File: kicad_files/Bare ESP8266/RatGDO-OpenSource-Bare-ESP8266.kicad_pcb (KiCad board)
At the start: 2 copper layers, 55 x 82.7 mm, 24 parts, among them J1 Screw_Terminal_01x03, J2 Screw_Terminal_01x03, J3 Screw_Terminal_01x03, J4 Conn_01x04, J5 Screw_Terminal_01x02, J6 Conn_01x02, Q1 2N7002, Q2 AO3400A, SW1 SW_Push, U1 ESP-12F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

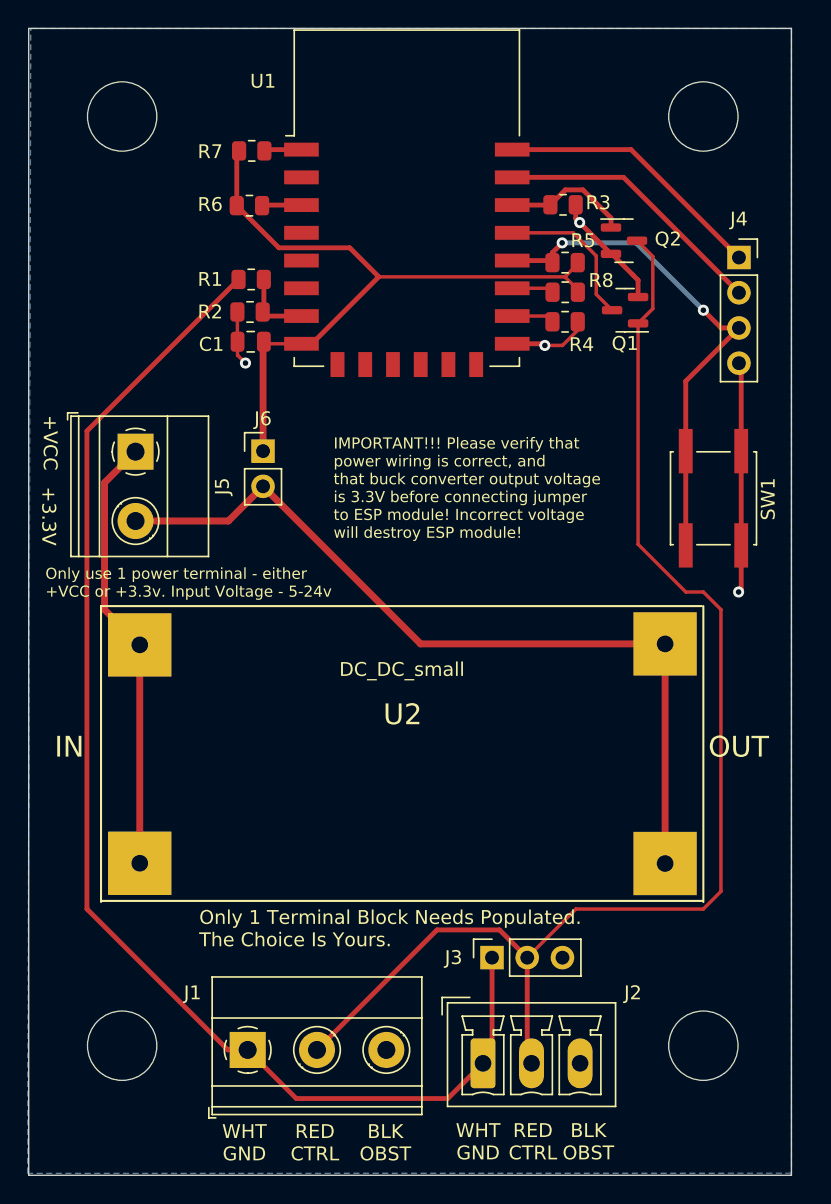
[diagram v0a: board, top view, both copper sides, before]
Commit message: Missed Silkscreening for programming header
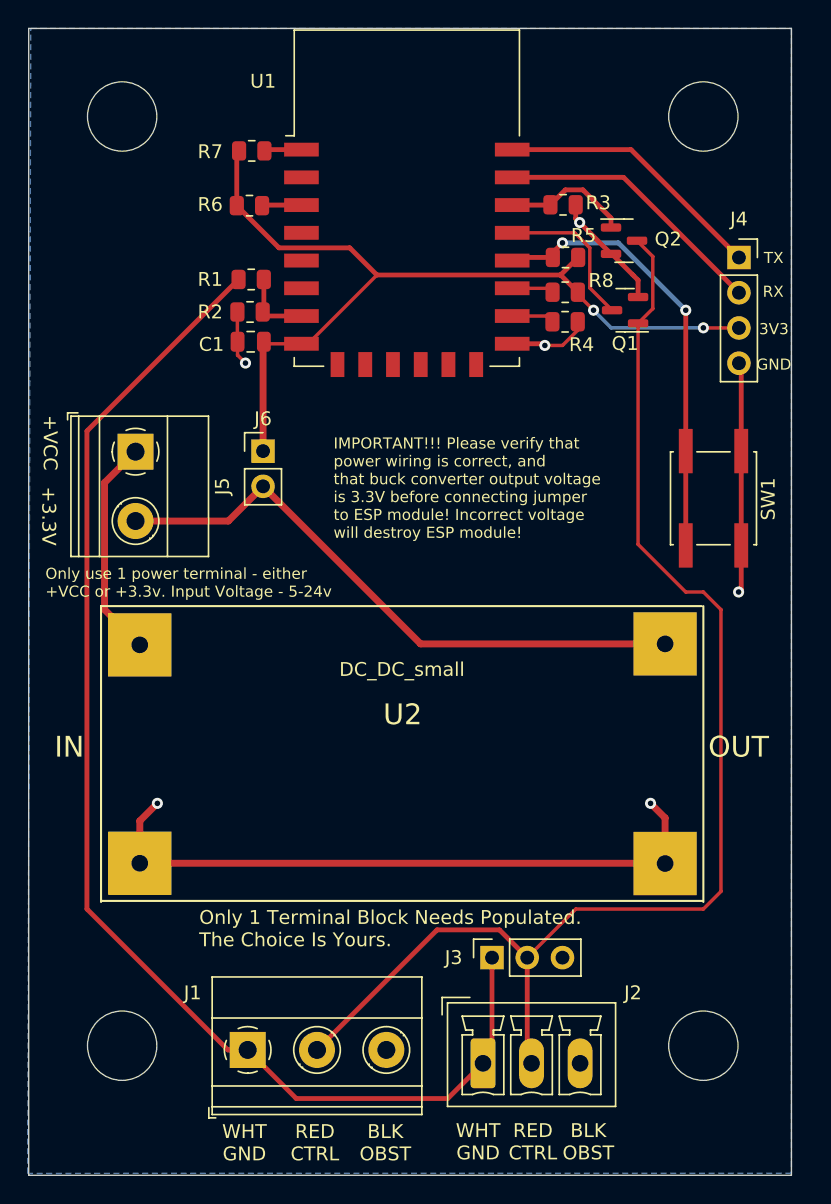
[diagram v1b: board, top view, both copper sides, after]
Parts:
- moved R5 0.38 mm to (152.6, 73.7)
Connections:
- J4 pad 3: Net-(J4-Pin_3) -> +3.3V
- R5 pad 1: Net-(J4-Pin_3) -> Net-(U1-GPIO0)
- SW1 pad 2: Net-(J4-Pin_3) -> Net-(U1-GPIO0)
- U1 pad 18: Net-(J4-Pin_3) -> Net-(U1-GPIO0)
- U2 pad 2: +12V -> GND
- U2 pad 4: Net-(J5-+3.3V) -> GND
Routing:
- net GND: track 35.2 -> 82.8 mm, vias 4 -> 6
- net Net-(J4-Pin_3): track 37.2 -> 0.00 mm, vias 2 -> 0
- net Net-(U1-GPIO0): track 0.00 -> 32.4 mm, vias 0 -> 2
- net Net-(J5-+3.3V): track 59.8 -> 43.9 mm
- net +12V: track 31.7 -> 15.9 mm
- net +3.3V: track 51.1 -> 65.1 mm, vias 0 -> 2
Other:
- board text added: "3V3"
- board text added: "GND"
- board text added: "RX"
- board text added: "TX"

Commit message: Updated Trace widths
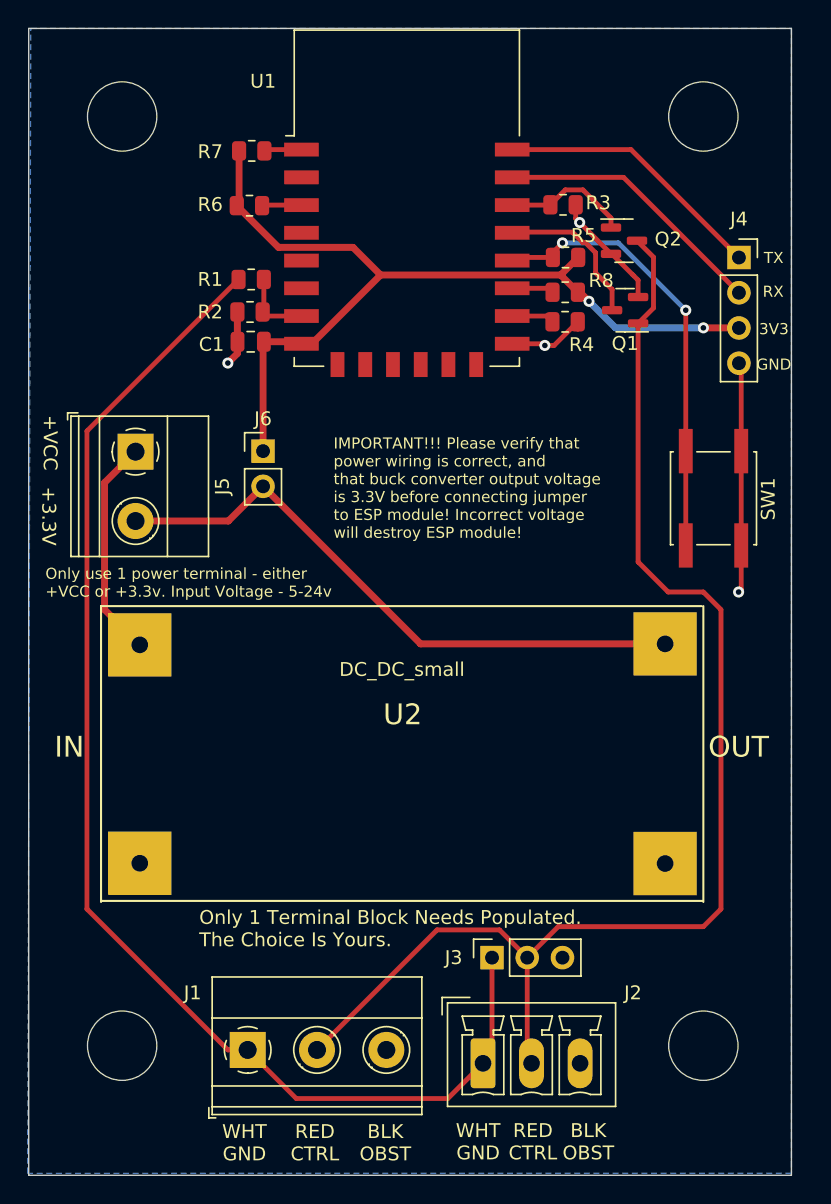
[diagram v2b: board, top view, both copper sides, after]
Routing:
- net GND: track 82.8 -> 35.6 mm, vias 6 -> 4
- net Net-(J1-RED/CTRL): track 94.3 -> 95.9 mm
- net +3.3V: track 65.1 -> 65.6 mm

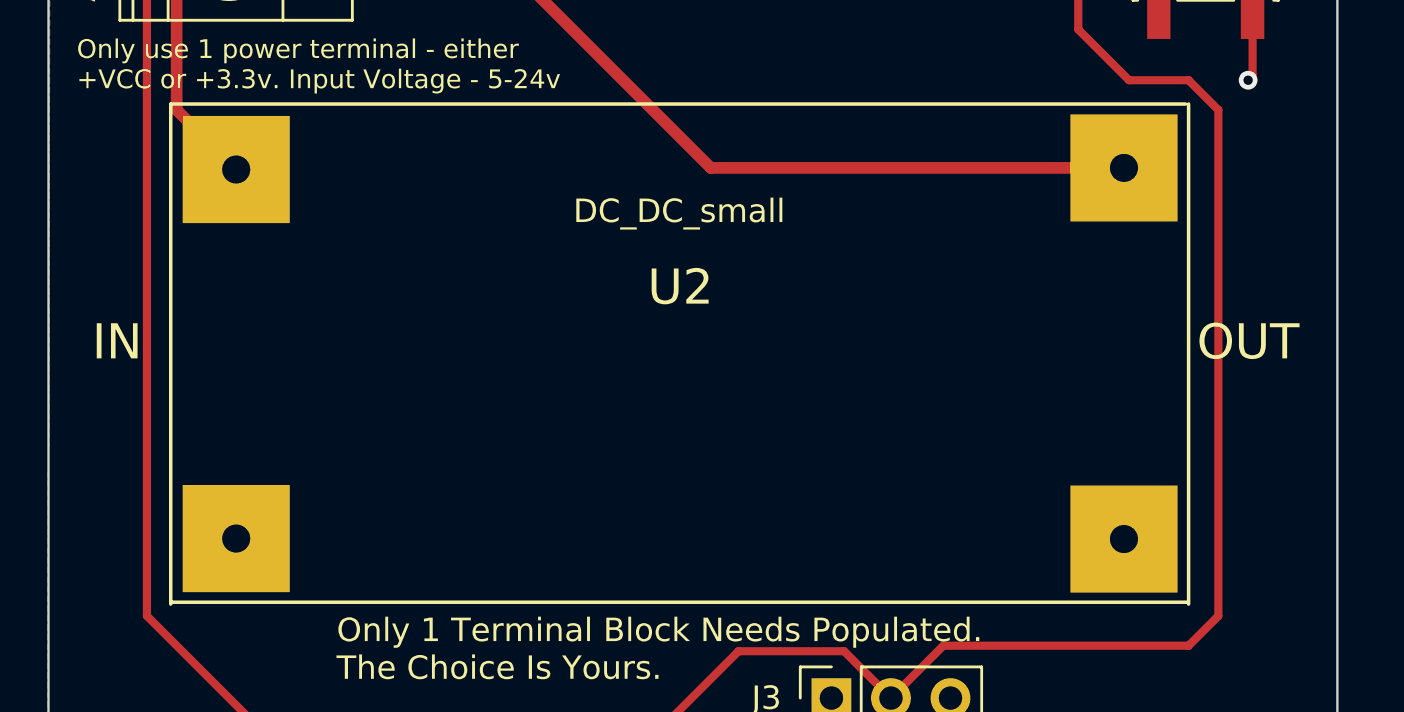
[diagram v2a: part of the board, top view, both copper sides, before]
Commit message: Added silkscreen to LM2596 area to aid in placement.
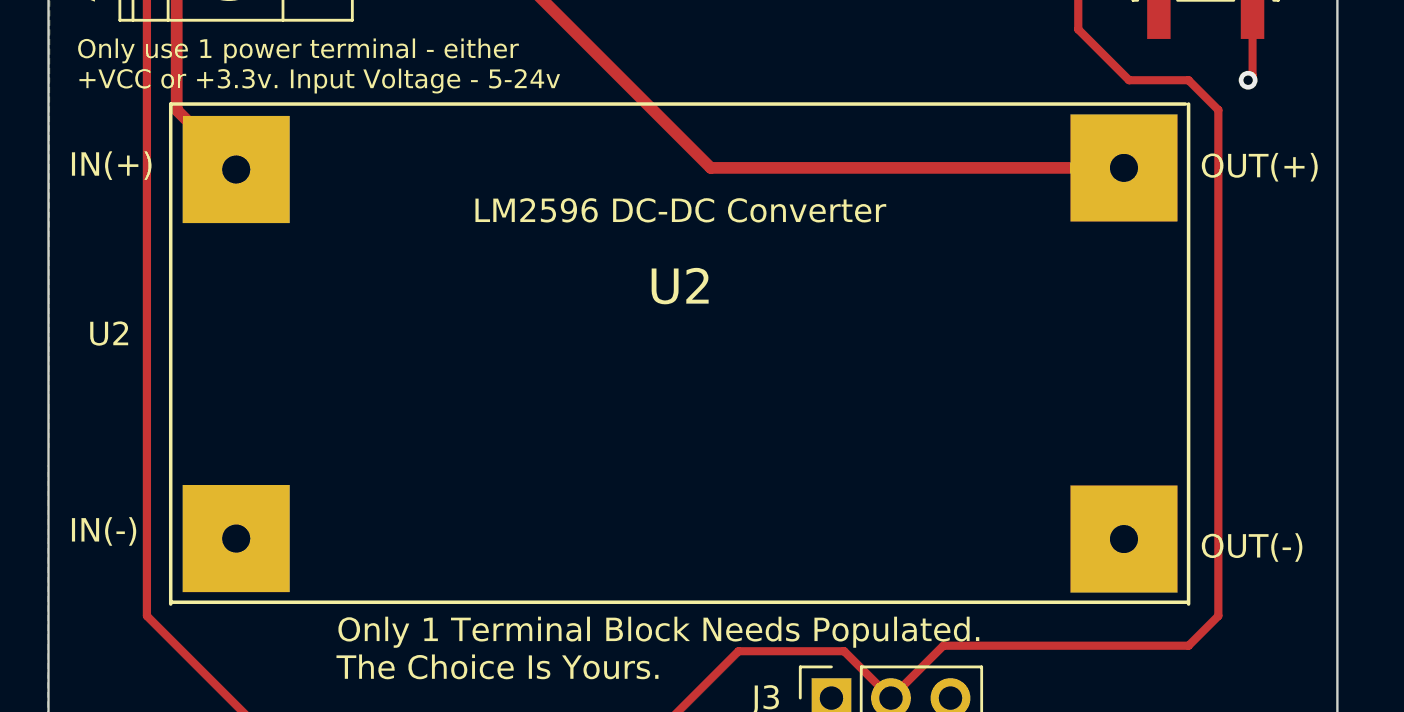
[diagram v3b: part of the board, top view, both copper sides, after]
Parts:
- U2: value DC_DC_small -> LM2596 DC-DC Converter
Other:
- board text added: "IN(+)"
- board text added: "IN(-)"
- board text added: "OUT(+)"
- board text added: "OUT(-)"
- board text added: "U2"
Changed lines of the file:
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@@
         (effects (font (size 1.5 1.5) (thickness 0.15)))
     )
-    (fp_text value "DC_DC_small" (at 0.0508 -5.588) (layer "F.SilkS")
-        (effects (font (size 1 1) (thickness 0.15)))
-    )
-    (fp_text user "IN" (at -23.9355 0) (layer "F.SilkS")
-        (effects (font (size 1.5 1.5) (thickness 0.15)))
-    )
-    (fp_text user "OUT" (at 24.3245 0) (layer "F.SilkS")
-        (effects (font (size 1.5 1.5) (thickness 0.15)))
+    (fp_text value "LM2596 DC-DC Converter" (at 0.0508 -5.588) (layer "F.SilkS")
+        (effects (font (size 1 1) (thickness 0.15)))
     )
     (fp_line (start -21.6495 -10.16) (end 21.6495 -10.16)
@@
     (effects (font (size 1 1) (thickness 0.15)) (justify bottom))
   )
+  (gr_text "IN(+)" (at 114.774765 101.986489) (layer "F.SilkS")
+    (effects (font (size 1 1) (thickness 0.15)) (justify left bottom))
+  )
   (gr_text "GND" (at 166.390265 81.852093) (layer "F.SilkS")
     (effects (font (size 0.8 0.8) (thickness 0.15)) (justify left bottom))
@@
     (effects (font (size 1 1) (thickness 0.15)) (justify left bottom))
   )
+  (gr_text "IN(-)" (at 114.774765 117.597697) (layer "F.SilkS")
+    (effects (font (size 1 1) (thickness 0.15)) (justify left bottom))
+  )
   (gr_text "BLK\nOBST" (at 139.626103 138.894836) (layer "F.SilkS")
     (effects (font (size 1 1) (thickness 0.15)) (justify bottom))
   )
+  (gr_text "U2" (at 115.57 109.22) (layer "F.SilkS")
+    (effects (font (size 1 1) (thickness 0.15)) (justify left bottom))
+  )
+  (gr_text "OUT(-)" (at 163.046266 118.2824) (layer "F.SilkS")
+    (effects (font (size 1 1) (thickness 0.15)) (justify left bottom))
+  )
   (gr_text "+VCC" (at 114.874616 85.028219 270) (layer "F.SilkS")
     (effects (font (size 1 1) (thickness 0.15)) (justify left bottom))
@@
     (effects (font (size 0.8 0.8) (thickness 0.15)) (justify left bottom))
   )
+  (gr_text "OUT(+)" (at 163.046266 102.054959) (layer "F.SilkS")
+    (effects (font (size 1 1) (thickness 0.15)) (justify left bottom))
+  )
   (gr_text "RX" (at 166.83659 76.597638) (layer "F.SilkS")

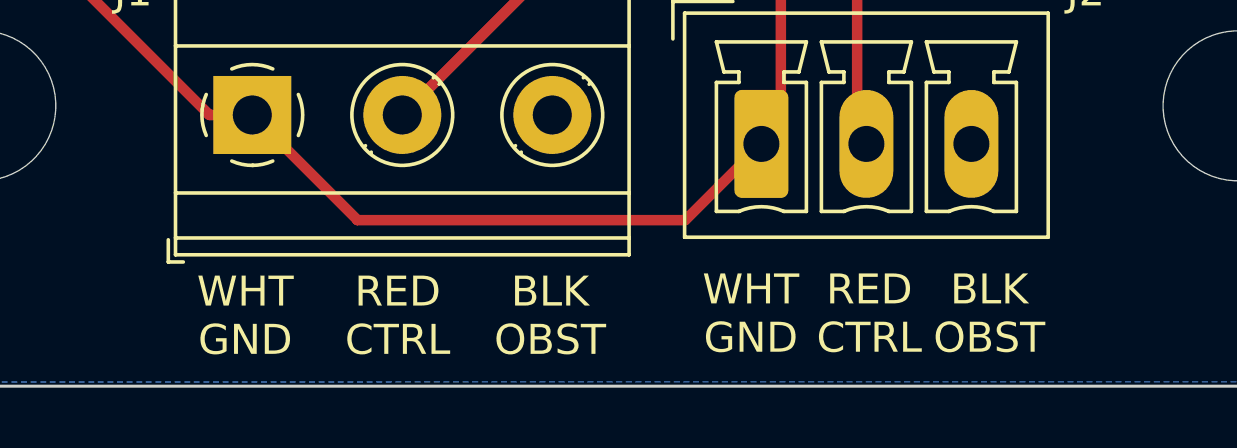
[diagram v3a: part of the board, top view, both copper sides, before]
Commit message: Fixed Silkscreen issue - positive and ground swap
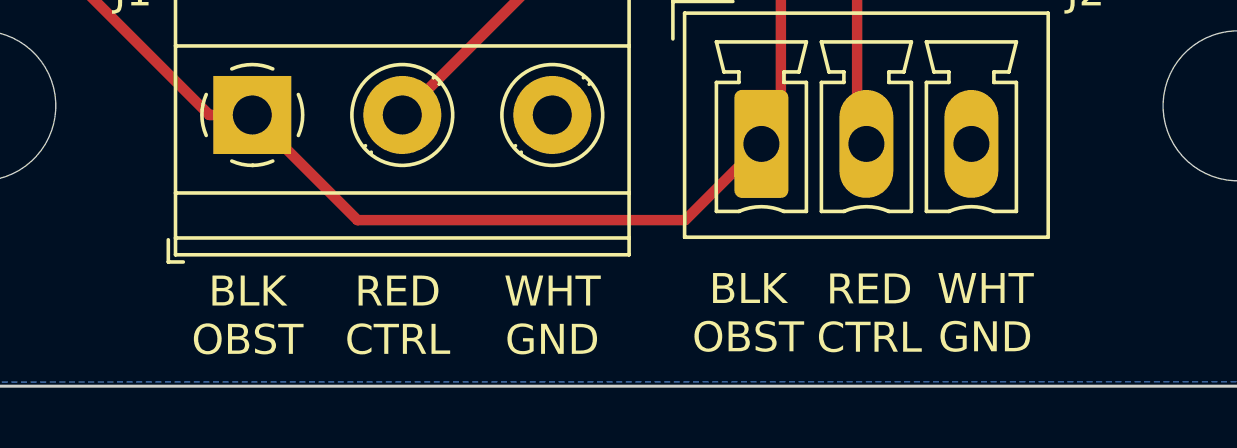
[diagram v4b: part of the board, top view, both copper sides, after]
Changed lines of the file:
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@@
   (gr_rect (start 113.91 57.15) (end 168.91 139.85)
     (stroke (width 0.1) (type default)) (fill none) (layer "Edge.Cuts"))
-  (gr_text "BLK\nOBST" (at 154.265587 138.824201) (layer "F.SilkS")
+  (gr_text "BLK\nOBST" (at 146.226739 138.809743) (layer "F.SilkS")
     (effects (font (size 1 1) (thickness 0.15)) (justify bottom))
   )
@@
     (effects (font (size 1 1) (thickness 0.15)) (justify bottom))
   )
-  (gr_text "WHT\nGND" (at 129.466103 138.894836) (layer "F.SilkS")
+  (gr_text "WHT\nGND" (at 139.7 138.894836) (layer "F.SilkS")
     (effects (font (size 1 1) (thickness 0.15)) (justify bottom))
   )
@@
     (effects (font (size 1 1) (thickness 0.15)) (justify left bottom))
   )
-  (gr_text "BLK\nOBST" (at 139.626103 138.894836) (layer "F.SilkS")
+  (gr_text "BLK\nOBST" (at 129.54 138.894836) (layer "F.SilkS")
     (effects (font (size 1 1) (thickness 0.15)) (justify bottom))
   )
@@
     (effects (font (size 1 1) (thickness 0.15)) (justify left bottom))
   )
-  (gr_text "WHT\nGND" (at 146.317376 138.824201) (layer "F.SilkS")
+  (gr_text "WHT\nGND" (at 154.135048 138.809743) (layer "F.SilkS")
     (effects (font (size 1 1) (thickness 0.15)) (justify bottom))
   )

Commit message: Update schematics for mini wide board v2.5
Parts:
- renumbered REF** to H1
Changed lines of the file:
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@@
     (descr "Mounting Hole 5mm, no annular")
     (tags "mounting hole 5mm no annular")
-    (attr exclude_from_pos_files exclude_from_bom)
-    (fp_text reference "REF**" (at 0 -6) (layer "F.SilkS") hide
+    (attr board_only exclude_from_pos_files exclude_from_bom)
+    (fp_text reference "H1" (at 0 -6) (layer "F.SilkS") hide
         (effects (font (size 1 1) (thickness 0.15)))
     )
@@
     (descr "Mounting Hole 5mm, no annular")
     (tags "mounting hole 5mm no annular")
-    (attr exclude_from_pos_files exclude_from_bom)
-    (fp_text reference "REF**" (at 0 -6) (layer "F.SilkS") hide
+    (attr board_only exclude_from_pos_files exclude_from_bom)
+    (fp_text reference "H1" (at 0 -6) (layer "F.SilkS") hide
         (effects (font (size 1 1) (thickness 0.15)))
     )
@@
     (descr "Mounting Hole 5mm, no annular")
     (tags "mounting hole 5mm no annular")
-    (attr exclude_from_pos_files exclude_from_bom)
-    (fp_text reference "REF**" (at 0 -6) (layer "F.SilkS") hide
+    (attr board_only exclude_from_pos_files exclude_from_bom)
+    (fp_text reference "H1" (at 0 -6) (layer "F.SilkS") hide
         (effects (font (size 1 1) (thickness 0.15)))
     )
@@
     (descr "Mounting Hole 5mm, no annular")
     (tags "mounting hole 5mm no annular")
-    (attr exclude_from_pos_files exclude_from_bom)
-    (fp_text reference "REF**" (at 0 -6) (layer "F.SilkS") hide
-        (effects (font (size 1 1) (thickness 0.15)))
-    )
+    (attr board_only exclude_from_pos_files exclude_from_bom)
+    (fp_text reference "H1" (at 0 -6) (layer "F.SilkS") hide
+        (effects (font (size 1 1) (thickness 0.15)))
+    )
